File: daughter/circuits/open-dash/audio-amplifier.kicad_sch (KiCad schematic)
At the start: 33 parts, among them J12 AudioJack_3.5TRS, J13 AudioJack_3.5TRS, J14 Conn_02x03_Odd_Even, J42 Terminal_01x04, J44 Terminal_01x04, J45 Terminal_01x04, T1 Audio_Transformer, T2 Audio_Transformer, T3 Audio_Transformer, T4 Audio_Transformer, U7 TDA7851F

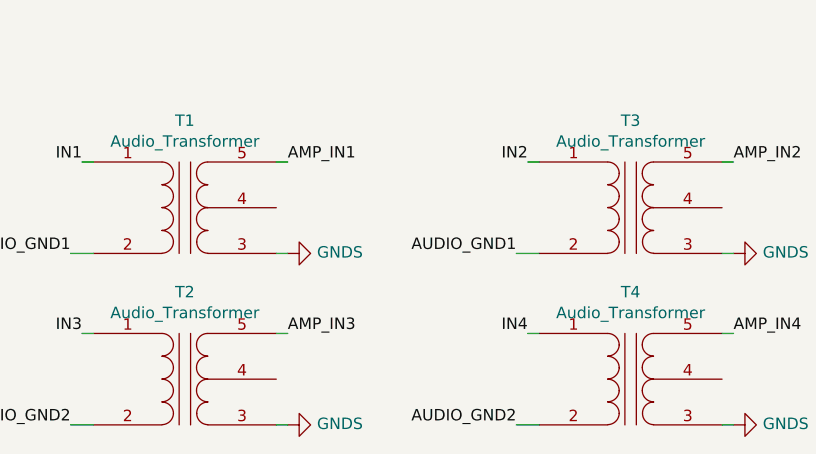
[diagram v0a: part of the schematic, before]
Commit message: Updated hvac circuit
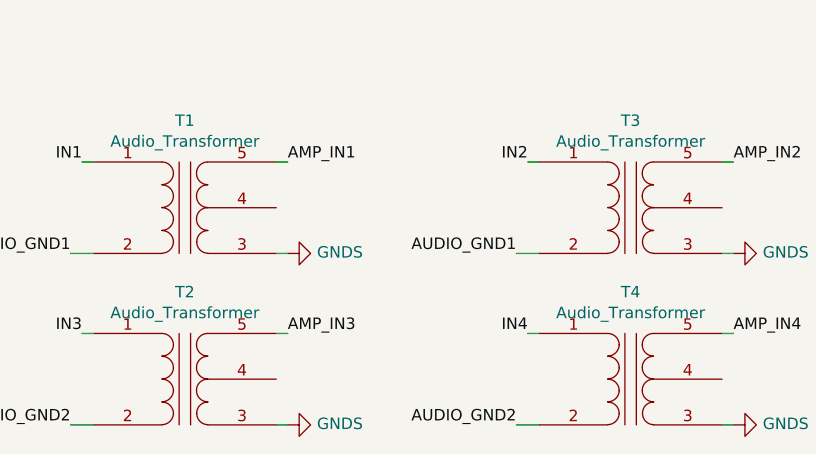
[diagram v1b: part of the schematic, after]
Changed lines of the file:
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@@
     (pin "2")
   )
-  (symbol (lib_id "Open_Automation:Terminal_01x04") (at 24.13 100.33 180)
+  (symbol (lib_id "Open_Automation:Terminal_01x04") (at 24.13 100.33 180) (unit 1)
     (in_bom yes) (on_board yes)
     (property "Reference" "J44" (id 0) (at 24.13 106.68 90)
@@
     (pin "4")
   )
-  (symbol (lib_id "Open_Automation:Terminal_01x04") (at 24.13 115.57 180)
+  (symbol (lib_id "Open_Automation:Terminal_01x04") (at 24.13 115.57 180) (unit 1)
     (in_bom yes) (on_board yes)
     (property "Reference" "J45" (id 0) (at 24.13 120.65 90)
@@
     (pin "4")
   )
-  (symbol (lib_id "Open_Automation:Terminal_01x04") (at 24.13 83.82 180)
+  (symbol (lib_id "Open_Automation:Terminal_01x04") (at 24.13 83.82 180) (unit 1)
     (in_bom yes) (on_board yes)
     (property "Reference" "J42" (id 0) (at 24.13 90.17 90)
